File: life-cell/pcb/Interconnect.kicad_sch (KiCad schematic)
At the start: 1 part, among them J4 Interconnect

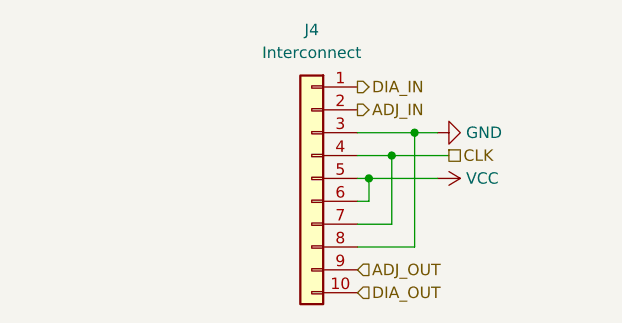
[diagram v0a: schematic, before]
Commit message: Switch to "symmetric" connector layout.
Each side has half male pins and half female pins, for a truly
symmetric experience!
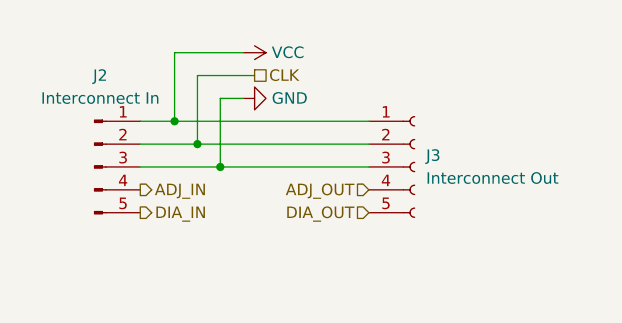
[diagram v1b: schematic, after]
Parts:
- removed J4: Interconnect, Connector_PinHeader_2.54mm:PinHeader_1x10_P2.54mm_Vertical, symbol Connector_Generic:Conn_01x10
- added J2: Interconnect In, Connector_PinHeader_2.54mm:PinHeader_1x05_P2.54mm_Horizontal, symbol Connector:Conn_01x05_Male
- added J3: Interconnect Out, Connector_PinSocket_2.54mm:PinSocket_1x05_P2.54mm_Horizontal, symbol Connector:Conn_01x05_Female
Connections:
- net ADJ_IN: now also J2.4 (Pin_4)
- net ADJ_OUT: now also J3.4 (Pin_4)
- net CLK: now also J2.2 (Pin_2), J3.2 (Pin_2)
- net DIA_IN: now also J2.5 (Pin_5)
- net DIA_OUT: now also J3.5 (Pin_5)
- net GND: now also J2.3 (Pin_3), J3.3 (Pin_3)
- net VCC: now also J2.1 (Pin_1), J3.1 (Pin_1)
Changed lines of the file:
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@@
 (kicad_sch (version 20211123) (generator eeschema)
   (paper "A4")
-  (junction (at 142.24 87.63) (diameter 0) (color 0 0 0 0)
+  (junction (at 125.73 86.36) (diameter 0) (color 0 0 0 0)
   )
-  (junction (at 144.78 85.09) (diameter 0) (color 0 0 0 0)
+  (junction (at 123.19 83.82) (diameter 0) (color 0 0 0 0)
   )
-  (junction (at 147.32 82.55) (diameter 0) (color 0 0 0 0)
+  (junction (at 120.65 81.28) (diameter 0) (color 0 0 0 0)
   )
-  (wire (pts (xy 140.97 95.25) (xy 147.32 95.25))
+  (wire (pts (xy 128.27 73.66) (xy 120.65 73.66))
     (stroke (width 0) (type default) (color 0 0 0 0))
   )
-  (wire (pts (xy 140.97 92.71) (xy 144.78 92.71))
+  (wire (pts (xy 120.65 73.66) (xy 120.65 81.28))
     (stroke (width 0) (type default) (color 0 0 0 0))
   )
-  (wire (pts (xy 140.97 90.17) (xy 142.24 90.17))
+  (wire (pts (xy 125.73 86.36) (xy 142.24 86.36))
     (stroke (width 0) (type default) (color 0 0 0 0))
   )
-  (wire (pts (xy 149.86 87.63) (xy 142.24 87.63))
+  (wire (pts (xy 116.84 86.36) (xy 125.73 86.36))
     (stroke (width 0) (type default) (color 0 0 0 0))
   )
-  (wire (pts (xy 142.24 87.63) (xy 142.24 90.17))
+  (wire (pts (xy 120.65 81.28) (xy 142.24 81.28))
     (stroke (width 0) (type default) (color 0 0 0 0))
   )
-  (wire (pts (xy 140.97 85.09) (xy 144.78 85.09))
+  (wire (pts (xy 128.27 78.74) (xy 125.73 78.74))
     (stroke (width 0) (type default) (color 0 0 0 0))
   )
-  (wire (pts (xy 144.78 85.09) (xy 151.13 85.09))
+  (wire (pts (xy 123.19 83.82) (xy 142.24 83.82))
     (stroke (width 0) (type default) (color 0 0 0 0))
   )
-  (wire (pts (xy 147.32 82.55) (xy 149.86 82.55))
+  (wire (pts (xy 123.19 76.2) (xy 123.19 83.82))
     (stroke (width 0) (type default) (color 0 0 0 0))
   )
-  (wire (pts (xy 140.97 82.55) (xy 147.32 82.55))
+  (wire (pts (xy 125.73 78.74) (xy 125.73 86.36))
     (stroke (width 0) (type default) (color 0 0 0 0))
   )
-  (wire (pts (xy 147.32 82.55) (xy 147.32 95.25))
+  (wire (pts (xy 116.84 81.28) (xy 120.65 81.28))
     (stroke (width 0) (type default) (color 0 0 0 0))
   )
-  (wire (pts (xy 140.97 87.63) (xy 142.24 87.63))
+  (wire (pts (xy 129.54 76.2) (xy 123.19 76.2))
     (stroke (width 0) (type default) (color 0 0 0 0))
   )
-  (wire (pts (xy 144.78 85.09) (xy 144.78 92.71))
+  (wire (pts (xy 116.84 83.82) (xy 123.19 83.82))
     (stroke (width 0) (type default) (color 0 0 0 0))
   )
-  (hierarchical_label "DIA_OUT" (shape input) (at 140.97 100.33 0)
+  (hierarchical_label "DIA_OUT" (shape input) (at 142.24 91.44 180)
+    (effects (font (size 1.27 1.27)) (justify right))
+  )
+  (hierarchical_label "ADJ_IN" (shape output) (at 116.84 88.9 0)
     (effects (font (size 1.27 1.27)) (justify left))
   )
-  (hierarchical_label "ADJ_IN" (shape output) (at 140.97 80.01 0)
+  (hierarchical_label "ADJ_OUT" (shape input) (at 142.24 88.9 180)
+    (effects (font (size 1.27 1.27)) (justify right))
+  )
+  (hierarchical_label "CLK" (shape passive) (at 129.54 76.2 0)
     (effects (font (size 1.27 1.27)) (justify left))
   )
-  (hierarchical_label "ADJ_OUT" (shape input) (at 140.97 97.79 0)
+  (hierarchical_label "DIA_IN" (shape output) (at 116.84 91.44 0)
     (effects (font (size 1.27 1.27)) (justify left))
   )
-  (hierarchical_label "CLK" (shape passive) (at 151.13 85.09 0)
-    (effects (font (size 1.27 1.27)) (justify left))
-  )
-  (hierarchical_label "DIA_IN" (shape output) (at 140.97 77.47 0)
-    (effects (font (size 1.27 1.27)) (justify left))
-  )
-  (symbol (lib_id "Connector_Generic:Conn_01x10") (at 135.89 87.63 0) (mirror y) (unit 1)
-    (in_bom yes) (on_board yes)
-    (property "Reference" "J4" (id 0) (at 135.89 71.12 0))
-    (property "Value" "Interconnect" (id 1) (at 135.89 73.66 0))
-    (property "Footprint" "Connector_PinHeader_2.54mm:PinHeader_1x10_P2.54mm_Vertical" (id 2) (at 135.89 87.63 0)
+  (symbol (lib_id "Connector:Conn_01x05_Female") (at 147.32 86.36 0) (unit 1)
+    (in_bom yes) (on_board yes) (fields_autoplaced)
+    (property "Reference" "J3" (id 0) (at 148.59 85.0899 0)
+      (effects (font (size 1.27 1.27)) (justify left))
+    )
+    (property "Value" "Interconnect Out" (id 1) (at 148.59 87.6299 0)
+      (effects (font (size 1.27 1.27)) (justify left))
+    )
+    (property "Footprint" "Connector_PinSocket_2.54mm:PinSocket_1x05_P2.54mm_Horizontal" (id 2) (at 147.32 86.36 0)
       (effects (font (size 1.27 1.27)) hide)
     )
-    (property "Datasheet" "~" (id 3) (at 135.89 87.63 0)
-      (effects (font (size 1.27 1.27)) hide)
-    )
-    (property "DigiKey" "" (id 4) (at 135.89 87.63 0)
-      (effects (font (size 1.27 1.27)) hide)
-    )
-    (property "Mfr" "" (id 5) (at 135.89 87.63 0)
-      (effects (font (size 1.27 1.27)) hide)
-    )
-    (property "P/N" "" (id 6) (at 135.89 87.63 0)
-      (effects (font (size 1.27 1.27)) hide)
-    )
-    (property "LCSC" "C188245 / C2897392" (id 7) (at 135.89 87.63 0)
+    (property "Datasheet" "~" (id 3) (at 147.32 86.36 0)
       (effects (font (size 1.27 1.27)) hide)
     )
     (pin "1")
-    (pin "10")
     (pin "2")
     (pin "3")
     (pin "4")
     (pin "5")
-    (pin "6")
-    (pin "7")
-    (pin "8")
-    (pin "9")
   )
-  (symbol (lib_id "power:VCC") (at 149.86 87.63 270) (unit 1)
+  (symbol (lib_id "power:VCC") (at 128.27 73.66 270) (mirror x) (unit 1)
     (in_bom yes) (on_board yes) (fields_autoplaced)
-    (property "Reference" "#PWR013" (id 0) (at 146.05 87.63 0)
+    (property "Reference" "#PWR014" (id 0) (at 124.46 73.66 0)
       (effects (font (size 1.27 1.27)) hide)
     )
-    (property "Value" "VCC" (id 1) (at 153.035 87.6299 90)
+    (property "Value" "VCC" (id 1) (at 131.445 73.6601 90)
       (effects (font (size 1.27 1.27)) (justify left))
     )
-    (property "Footprint" "" (id 2) (at 149.86 87.63 0)
+    (property "Footprint" "" (id 2) (at 128.27 73.66 0)
       (effects (font (size 1.27 1.27)) hide)
     )
-    (property "Datasheet" "" (id 3) (at 149.86 87.63 0)
+    (property "Datasheet" "" (id 3) (at 128.27 73.66 0)
       (effects (font (size 1.27 1.27)) hide)
     )
     (pin "1")
   )
-  (symbol (lib_id "power:GND") (at 149.86 82.55 90) (unit 1)
+  (symbol (lib_id "power:GND") (at 128.27 78.74 90) (mirror x) (unit 1)
     (in_bom yes) (on_board yes) (fields_autoplaced)
-    (property "Reference" "#PWR014" (id 0) (at 156.21 82.55 0)
+    (property "Reference" "#PWR013" (id 0) (at 134.62 78.74 0)
       (effects (font (size 1.27 1.27)) hide)
     )
-    (property "Value" "GND" (id 1) (at 153.035 82.5499 90)
+    (property "Value" "GND" (id 1) (at 131.445 78.7401 90)
       (effects (font (size 1.27 1.27)) (justify right))
     )
-    (property "Footprint" "" (id 2) (at 149.86 82.55 0)
+    (property "Footprint" "" (id 2) (at 128.27 78.74 0)
       (effects (font (size 1.27 1.27)) hide)
     )
-    (property "Datasheet" "" (id 3) (at 149.86 82.55 0)
+    (property "Datasheet" "" (id 3) (at 128.27 78.74 0)
       (effects (font (size 1.27 1.27)) hide)
     )
     (pin "1")
   )
+  (symbol (lib_id "Connector:Conn_01x05_Male") (at 111.76 86.36 0) (unit 1)
+    (in_bom yes) (on_board yes) (fields_autoplaced)
+    (property "Reference" "J2" (id 0) (at 112.395 76.2 0))
+    (property "Value" "Interconnect In" (id 1) (at 112.395 78.74 0))
+    (property "Footprint" "Connector_PinHeader_2.54mm:PinHeader_1x05_P2.54mm_Horizontal" (id 2) (at 111.76 86.36 0)
+      (effects (font (size 1.27 1.27)) hide)
+    )
+    (property "Datasheet" "~" (id 3) (at 111.76 86.36 0)
+      (effects (font (size 1.27 1.27)) hide)
+    )
+    (pin "1")
+    (pin "2")
+    (pin "3")
+    (pin "4")
+    (pin "5")
+  )
 )
